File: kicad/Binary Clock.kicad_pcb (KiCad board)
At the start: 2 copper layers, 172.7 x 111.8 mm, 63 parts, among them J1 AVR-ISP-10, J2 UART, J3 COM/TW, SW1 INC_HOUR, SW2 INC_MINUTE, SW3 INC_SECOND, SW4 INC_BTNESS, U1 ATmega32A-PU, U2 PCF8583P, Y1 32768hZ

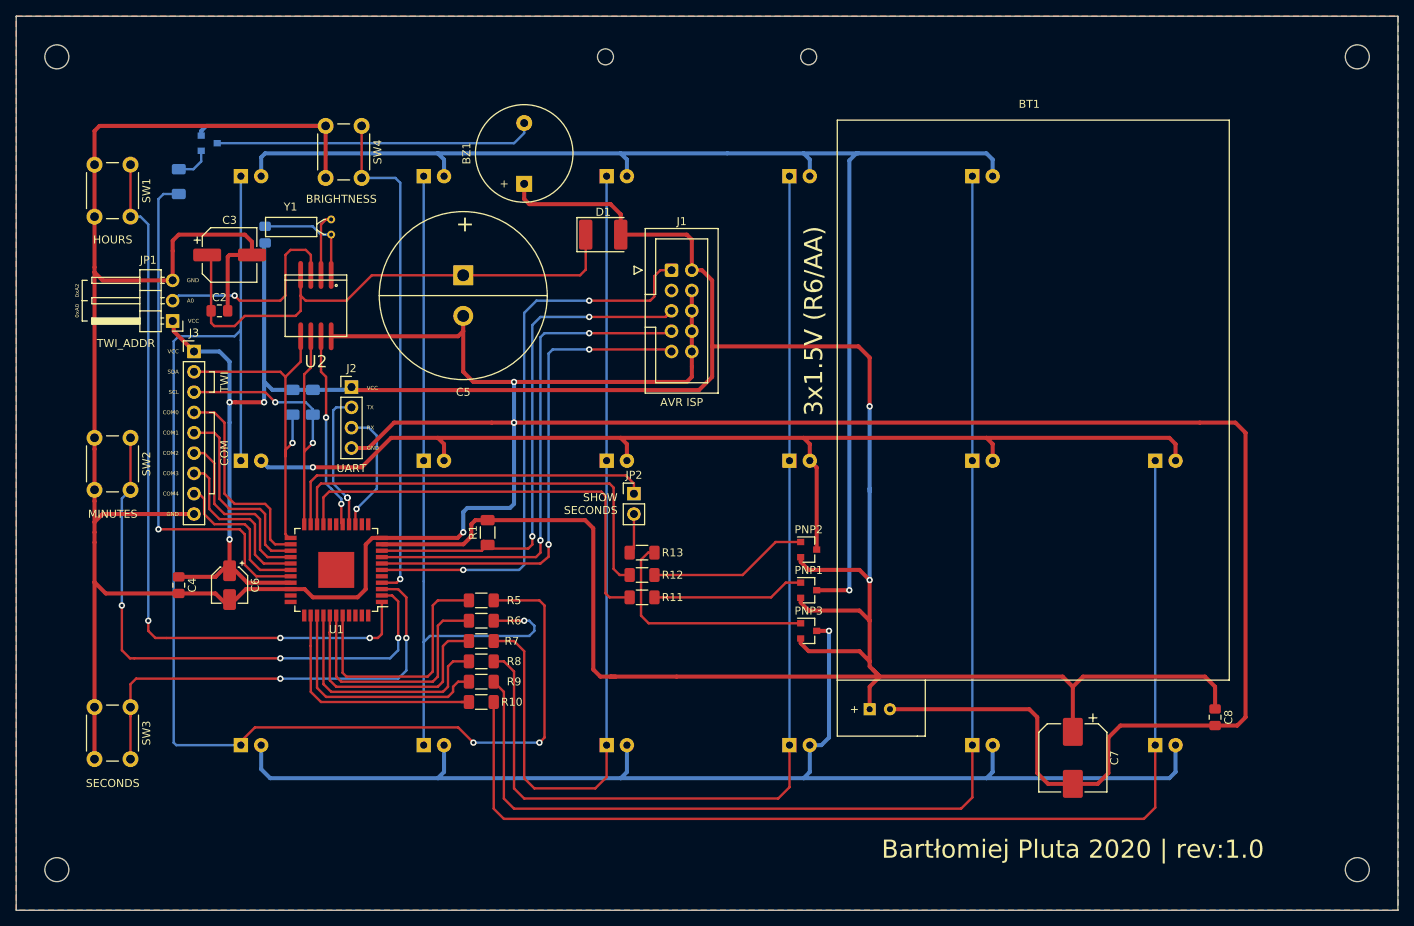
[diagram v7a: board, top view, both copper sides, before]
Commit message: Fix some issues and text labels on PCB
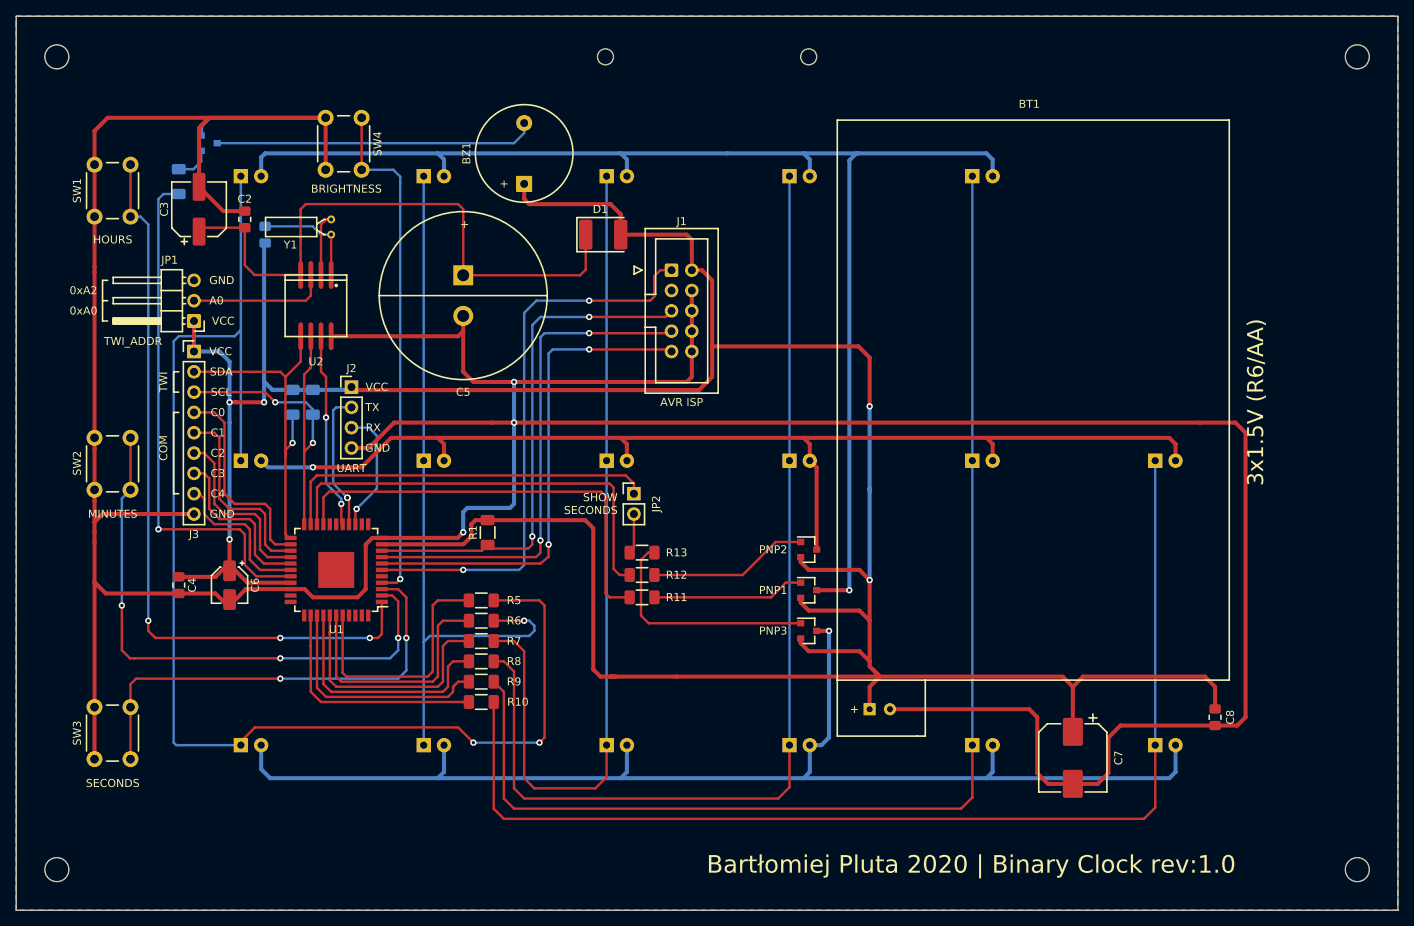
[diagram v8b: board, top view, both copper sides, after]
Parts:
- moved C2 11.9 mm to (89.5, 76.2), turned to 90 degrees
- moved C3 6.87 mm to (83.8, 74.9), turned to 90 degrees
- moved JP1 2.67 mm to (83.2, 88.9)
- moved SW4 1.02 mm to (104.1, 63.5)
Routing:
- net GND: track 533.1 -> 512.9 mm
- net Net-(JP1-Pad2): track 26.0 -> 17.5 mm, vias 1 -> 0
- net Net-(C2-Pad1): track 67.8 -> 75.4 mm
- net VCC: track 410.8 -> 409.7 mm
- net /INC_BTNESS: track 63.6 -> 64.5 mm
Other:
- board text added: "Bartłomiej Pluta 2020 | Binary Clock rev:1.0"
- board text added: "C0"
- board text added: "C1"
- board text added: "C2"
- board text added: "C3"
- board text added: "C4"
- board text removed: "Bartłomiej Pluta 2020 | rev:1.0"
- board text removed: "COM0"
- board text removed: "COM1"
- board text removed: "COM2"
- board text removed: "COM3"
- board text removed: "COM4"
